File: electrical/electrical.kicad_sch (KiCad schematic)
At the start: 0 parts

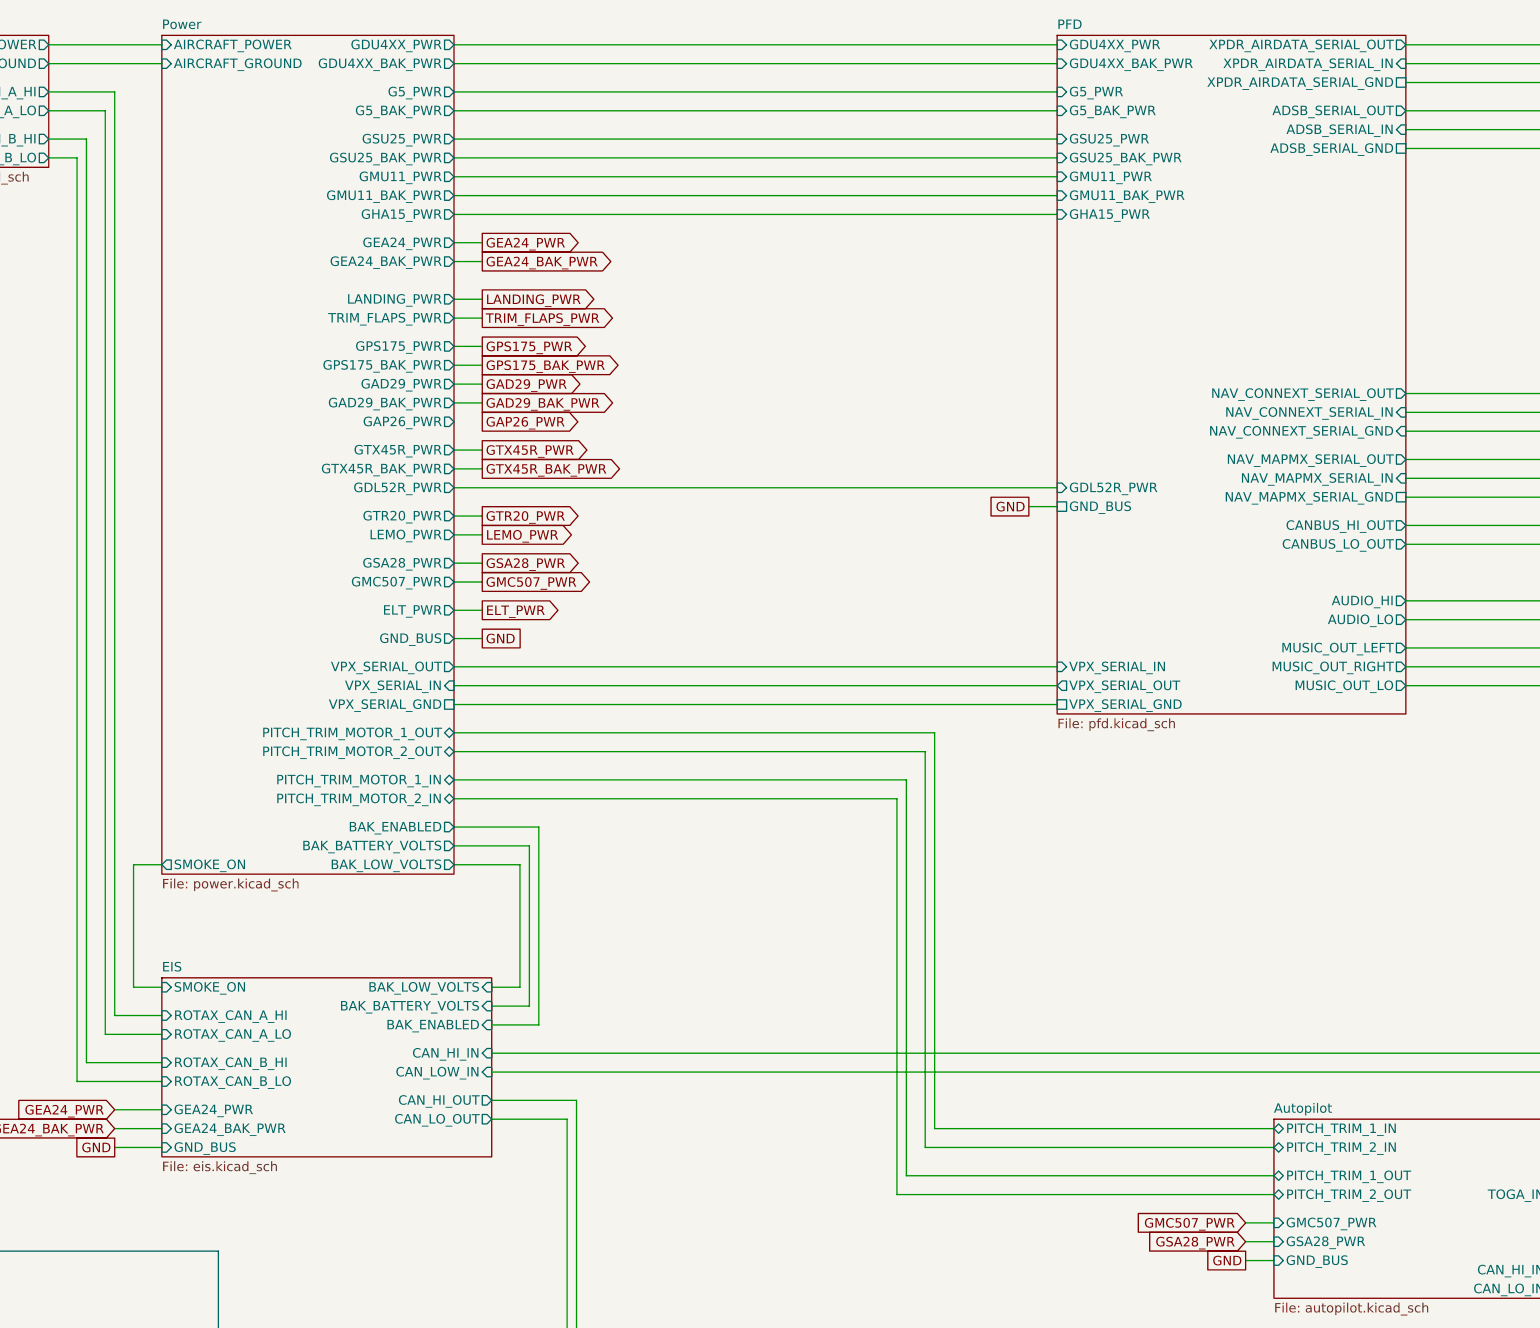
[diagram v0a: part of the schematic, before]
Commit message: Removed lights & trim/flaps power coming out of power overview. Renamed position to nav.
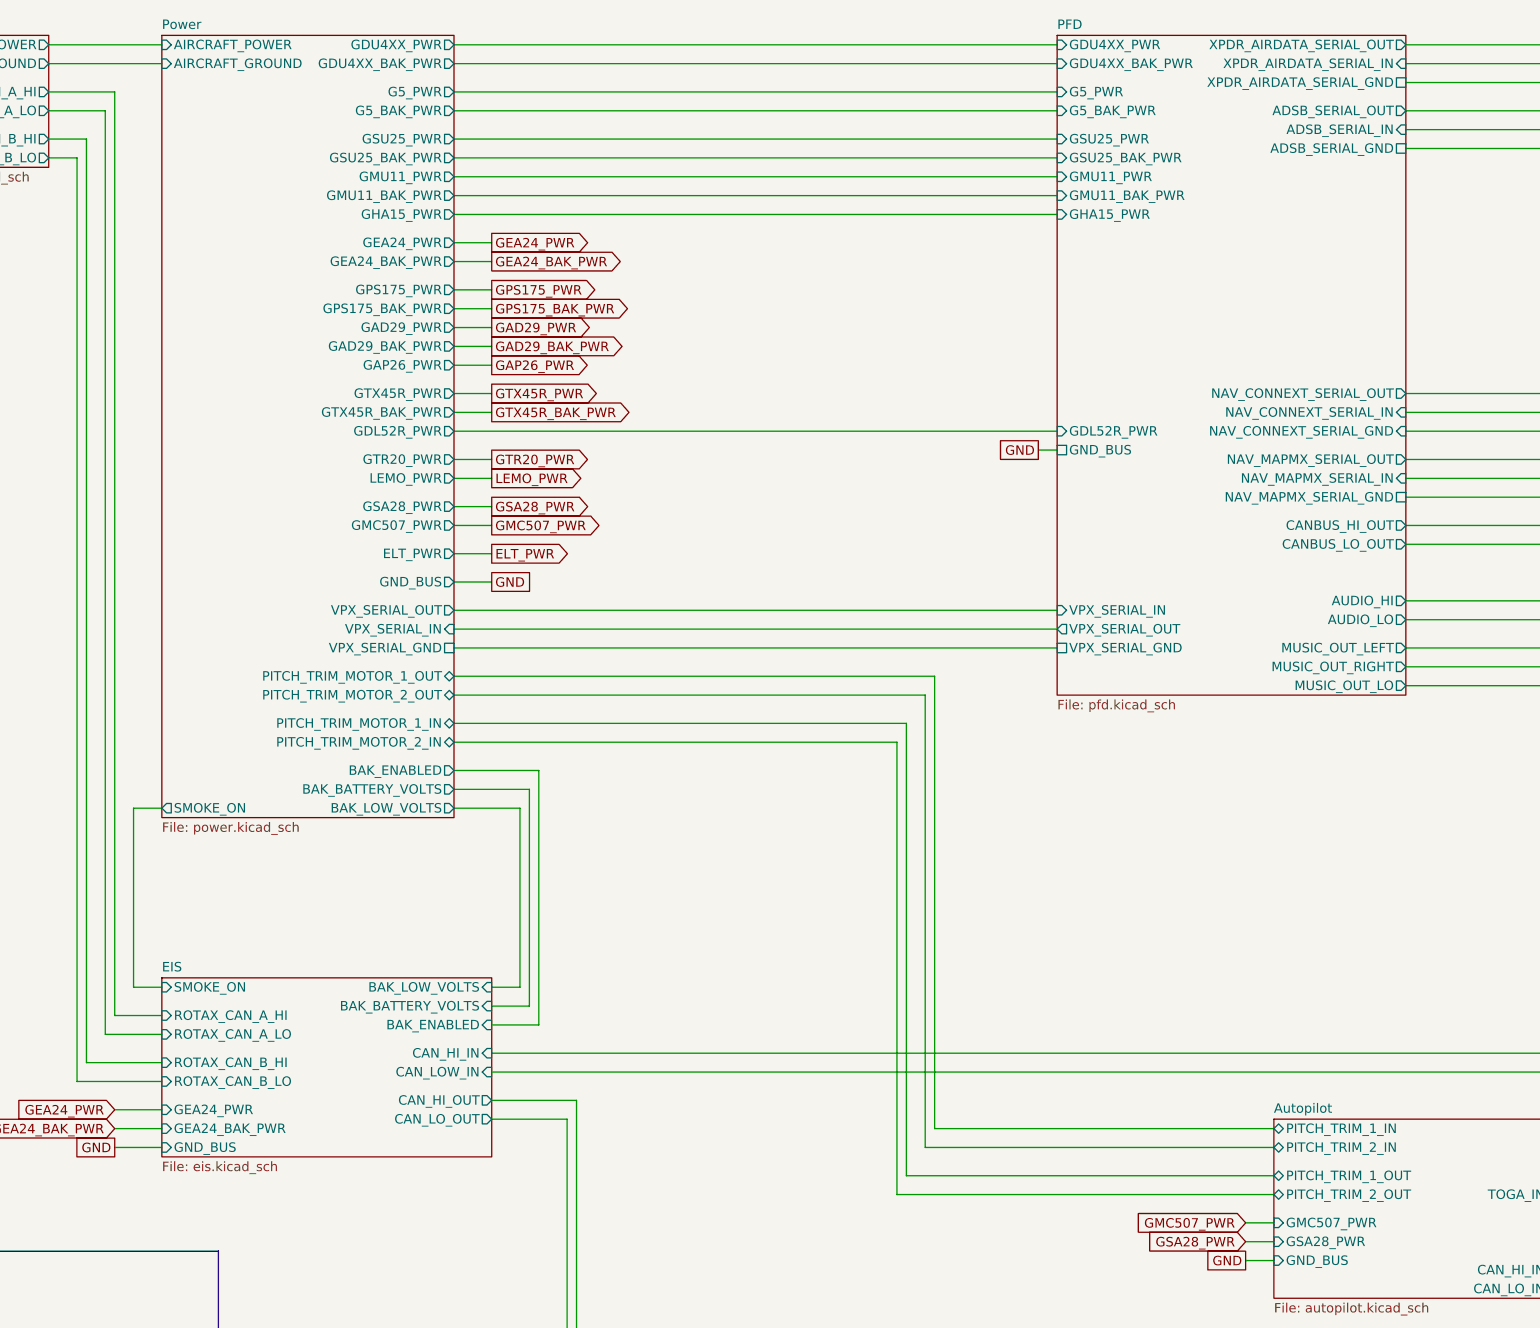
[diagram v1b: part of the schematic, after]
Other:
- sheet Power ports: added none; removed LANDING_PWR, TRIM_FLAPS_PWR

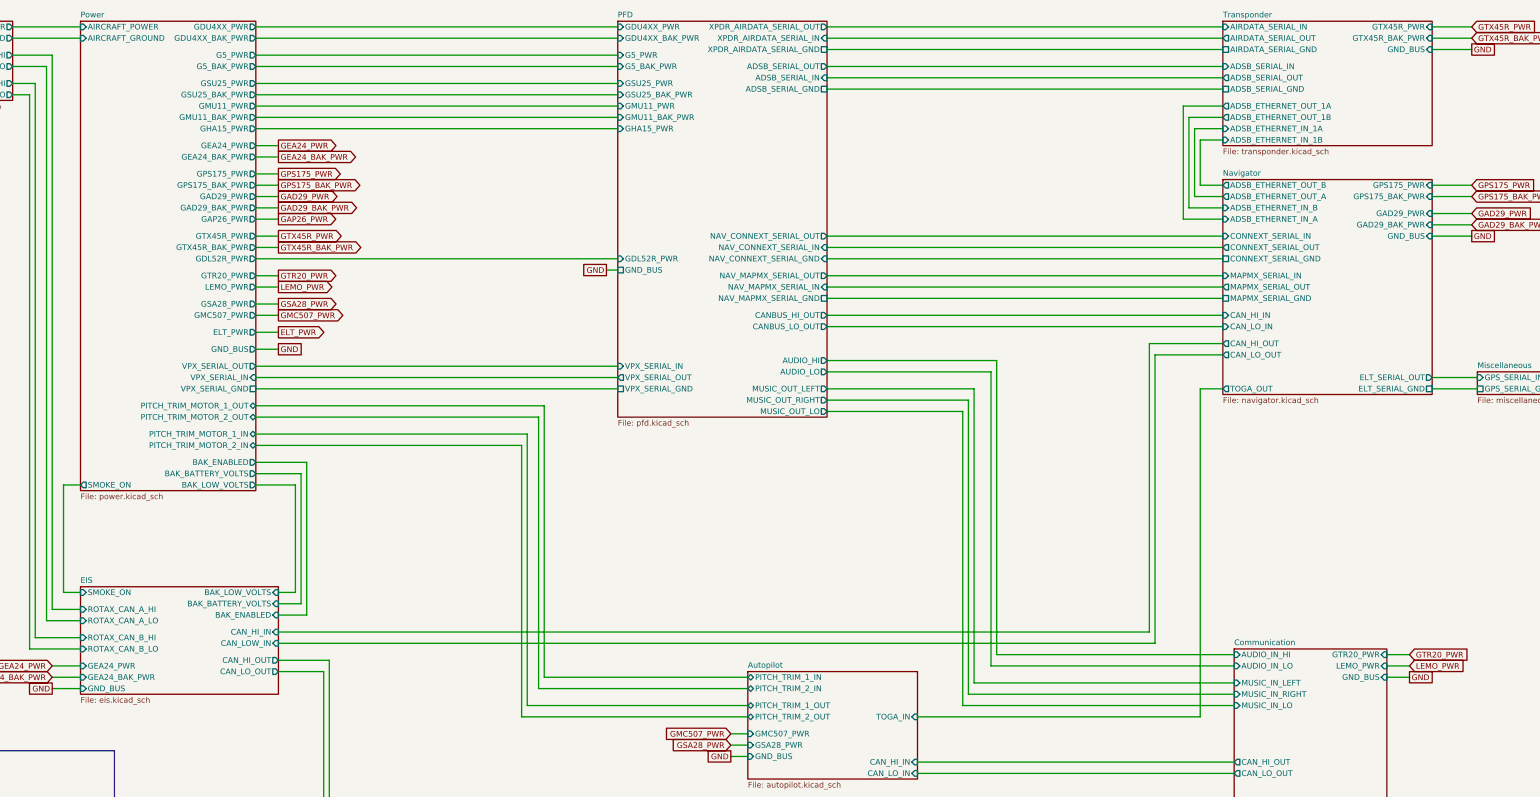
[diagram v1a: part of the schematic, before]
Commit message: Added bluetooth
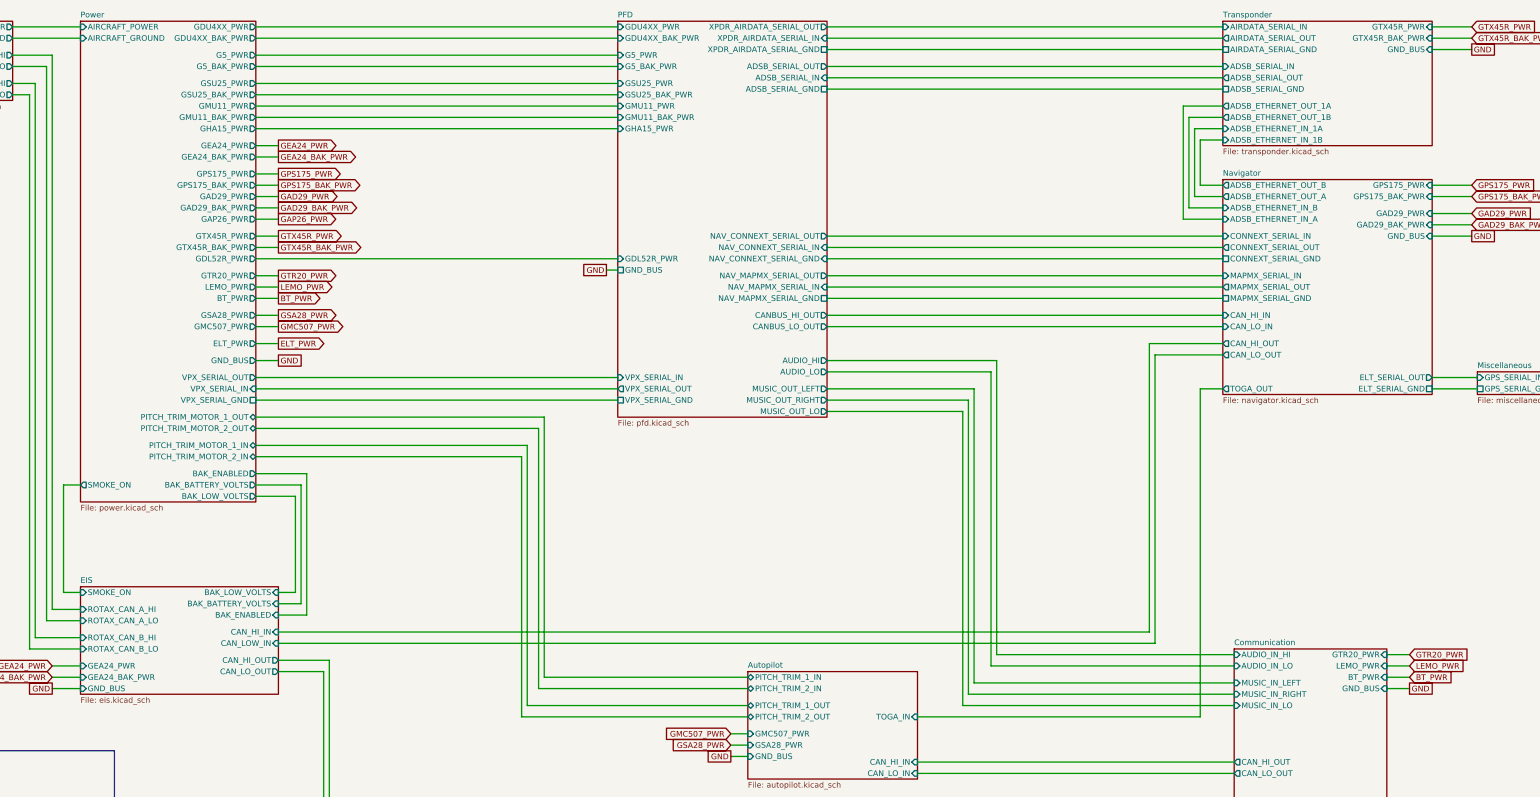
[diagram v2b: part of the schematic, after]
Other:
- sheet Communication ports: added BT_PWR; removed none
- sheet Power ports: added BT_PWR; removed none

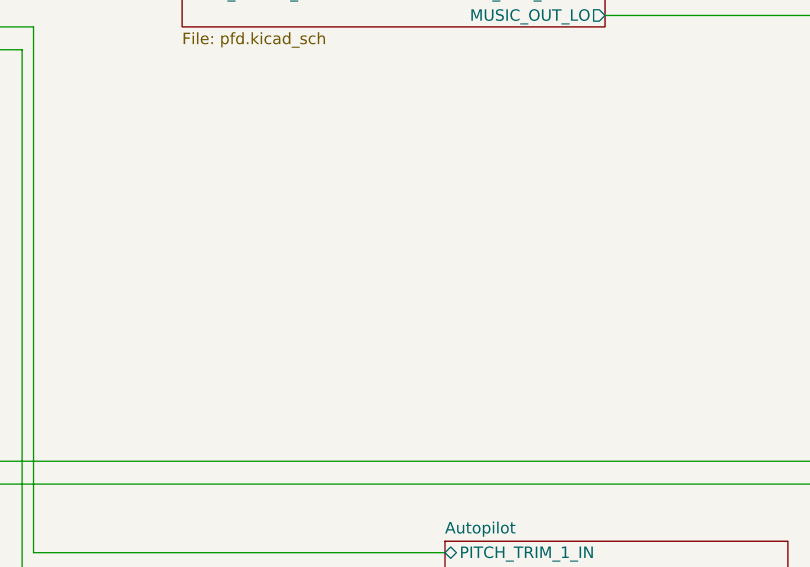
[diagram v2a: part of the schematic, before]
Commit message: Converted to breakers w/GAD 27 instead of VP-X.
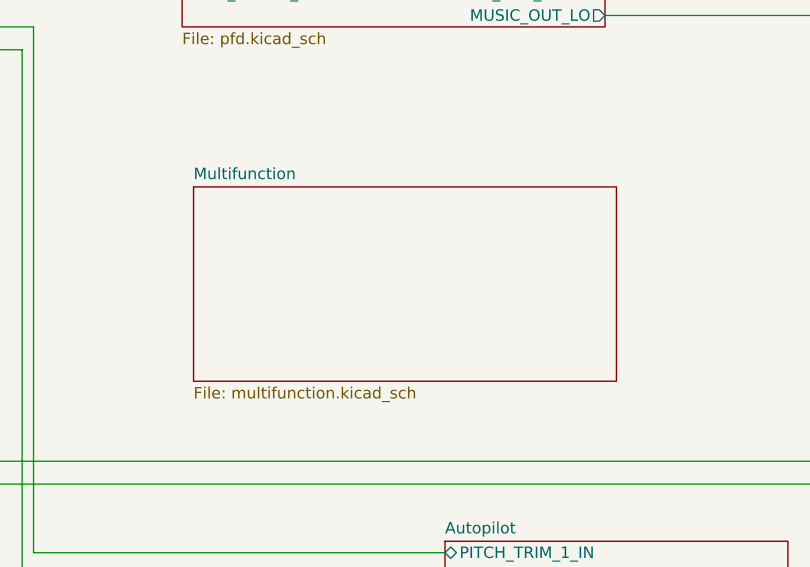
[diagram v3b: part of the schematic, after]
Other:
- added sheet Multifunction (multifunction.kicad_sch)
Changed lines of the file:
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@@
     (title "Electrical Overview")
     (date "2024-03-15")
-    (rev "0.9.2")
+    (rev "1.0")
     (company "N915SN Angry Bird")
+    (comment 1 "w/Breakers")
   )
   (wire (pts (xy 293.37 101.6) (xy 293.37 166.37))
@@
     )
   )
+  (sheet (at 175.26 135.89) (size 46.99 21.59) (fields_autoplaced)
+    (stroke (width 0.1524) (type solid))
+    (fill (color 0 0 0 0.0000))
+    (property "Sheetname" "Multifunction" (at 175.26 135.1784 0)
+      (effects (font (size 1.27 1.27)) (justify left bottom))
+    )
+    (property "Sheetfile" "multifunction.kicad_sch" (at 175.26 158.0646 0)
+      (effects (font (size 1.27 1.27)) (justify left top))
+    )
+    (instances
+      (project "electrical"
+        (path "/e8ec215a-dbe2-4eba-a577-e50a0a128049" (page "7"))
+      )
+    )
+  )
   (sheet (at 53.34 29.21) (size 39.37 107.95) (fields_autoplaced)
     (stroke (width 0.1524) (type solid))
@@
     (instances
       (project "electrical"
-        (path "/e8ec215a-dbe2-4eba-a577-e50a0a128049" (page "8"))
+        (path "/e8ec215a-dbe2-4eba-a577-e50a0a128049" (page "9"))
       )
     )
@@
     (instances
       (project "electrical"
-        (path "/e8ec215a-dbe2-4eba-a577-e50a0a128049" (page "11"))
+        (path "/e8ec215a-dbe2-4eba-a577-e50a0a128049" (page "12"))
       )
     )
@@
     (instances
       (project "electrical"
-        (path "/e8ec215a-dbe2-4eba-a577-e50a0a128049" (page "9"))
+        (path "/e8ec215a-dbe2-4eba-a577-e50a0a128049" (page "10"))
       )
     )
@@
     (instances
       (project "electrical"
-        (path "/e8ec215a-dbe2-4eba-a577-e50a0a128049" (page "10"))
+        (path "/e8ec215a-dbe2-4eba-a577-e50a0a128049" (page "11"))
       )
     )
@@
     (instances
       (project "electrical"
-        (path "/e8ec215a-dbe2-4eba-a577-e50a0a128049" (page "7"))
+        (path "/e8ec215a-dbe2-4eba-a577-e50a0a128049" (page "8"))
       )
     )

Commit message: Unknown set of changes. Didn't spent time to look
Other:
- sheet Autopilot ports: added GMC507_BAK_PWR; removed PITCH_TRIM_1_IN, PITCH_TRIM_1_OUT, PITCH_TRIM_2_IN, PITCH_TRIM_2_OUT
- sheet Multifunction ports: added CAN_HI_IN, CAN_HI_OUT, CAN_LO_IN, CAN_LO_OUT, GAD27_PWR, GND_BUS, LIGHT_PWR, SMOKE_PWR, TRIM_PWR; removed none
- sheet Power ports: added GAD27_PWR, GMC507_BAK_PWR, LANDING_LIGHTS_PWR, SMOKE_PWR, TRIM_PWR; removed PITCH_TRIM_MOTOR_1_IN, PITCH_TRIM_MOTOR_1_OUT, PITCH_TRIM_MOTOR_2_IN, PITCH_TRIM_MOTOR_2_OUT

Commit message: Interim check-in. Not sure what I was doing.
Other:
- removed sheet Multifunction
- sheet PFD ports: added none; removed VPX_SERIAL_GND, VPX_SERIAL_IN, VPX_SERIAL_OUT
- sheet Power ports: added none; removed GAD27_PWR, LANDING_LIGHTS_PWR, SMOKE_PWR, TRIM_PWR, VPX_SERIAL_GND, VPX_SERIAL_IN, VPX_SERIAL_OUT

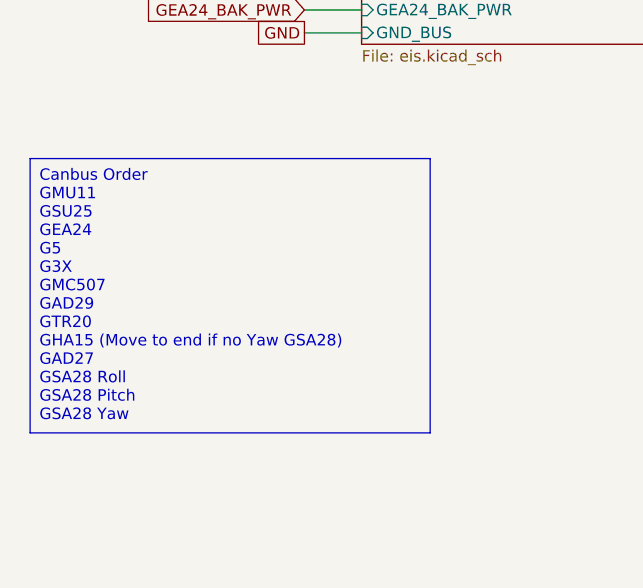
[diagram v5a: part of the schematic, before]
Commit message: Cleaned up power and smoke.
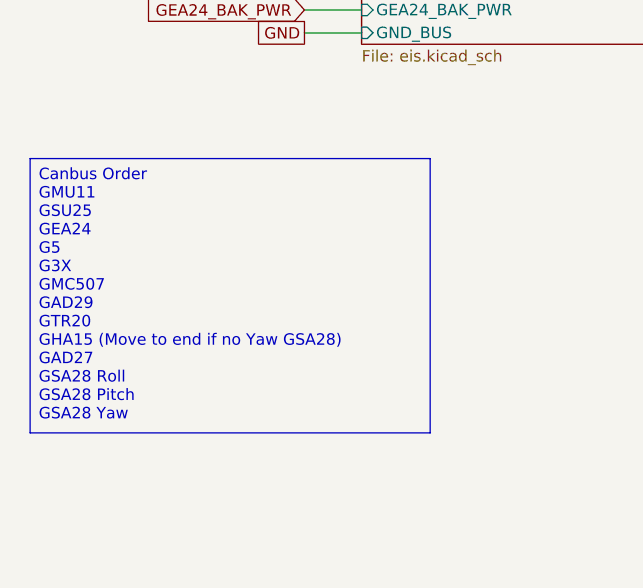
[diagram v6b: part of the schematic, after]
